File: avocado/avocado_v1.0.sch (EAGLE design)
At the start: 113 parts, among them IC1 TM4C129XXXPDT, IC3 MAX31855, IC4 ISO3088, J1 1X2-3.5MM, U1 LMT87DCKT

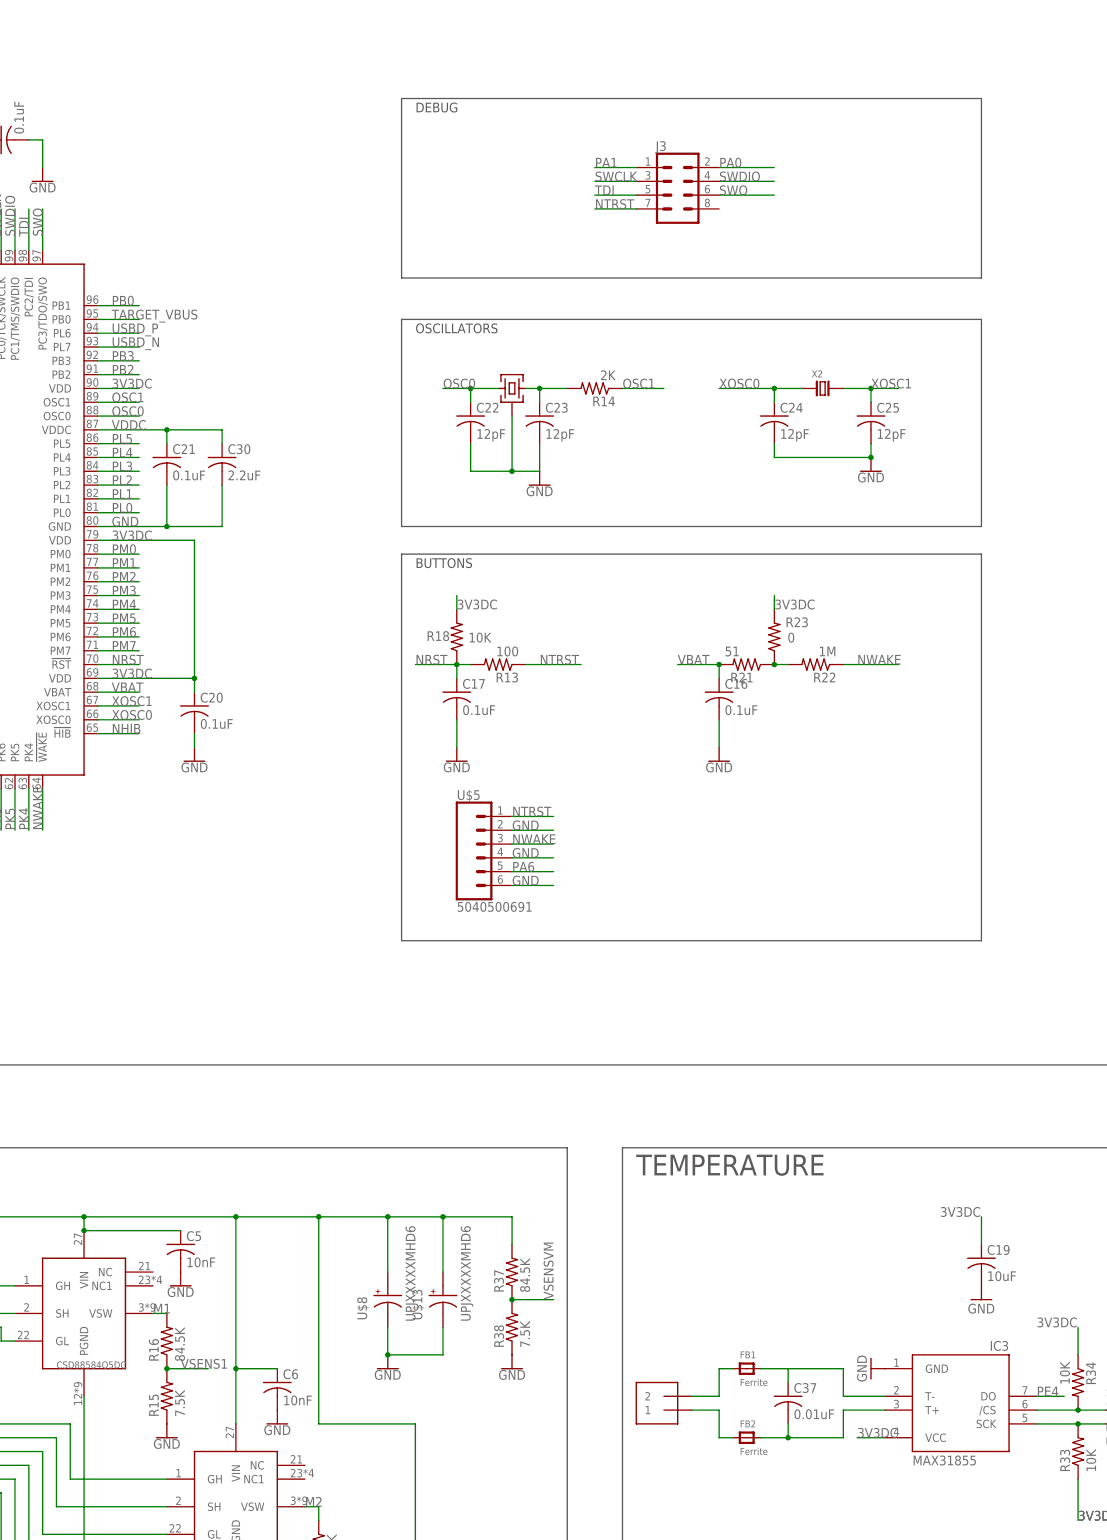
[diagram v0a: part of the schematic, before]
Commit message: expanded power and motor traces
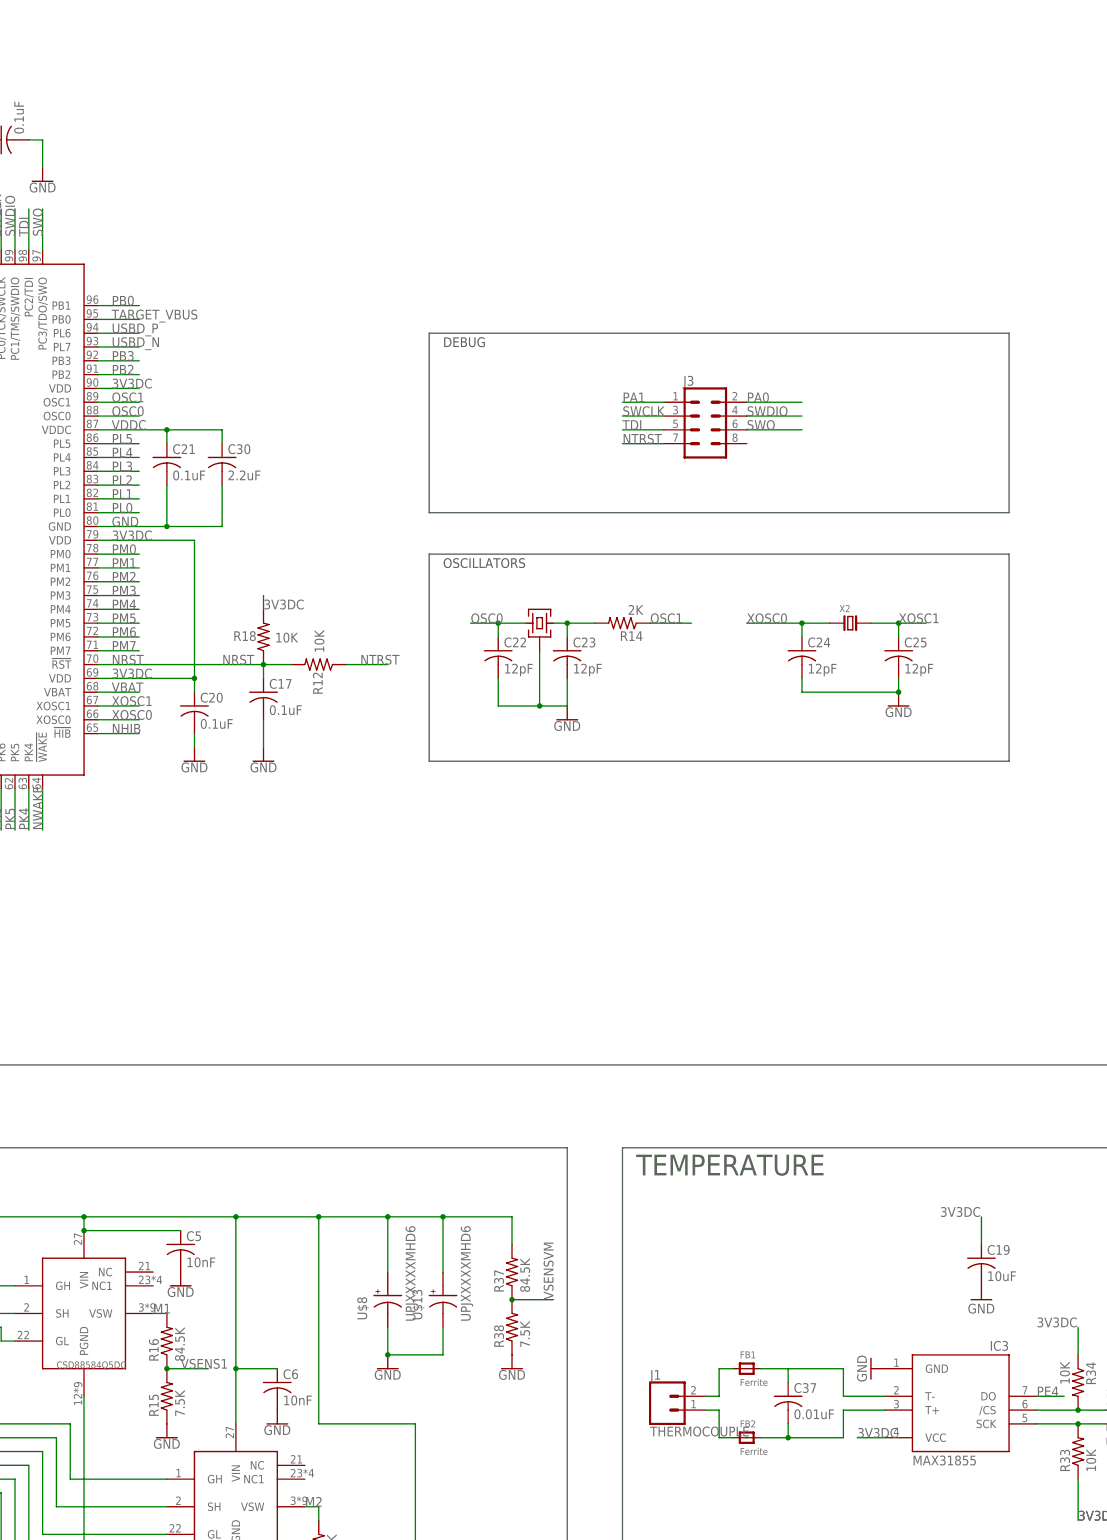
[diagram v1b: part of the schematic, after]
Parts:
- removed C16: 0.1uF, rcl:C-USC0402
- removed R13: 100, rcl:R-US_R0402
- removed R21: 51, rcl:R-US_R0402
- removed R22: 1M, rcl:R-US_R0402
- removed R23: 0, rcl:R-US_R0402
- removed U$5: 5040500691, avocado:5040500691
- added R12: 10K, rcl:R-US_R0402
- J1: value 1X2-3.5MM -> THERMOCOUPLE; device adafruit:1X2-3.5MM -> avocado:THERMOCOUPLE
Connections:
- removed net N$44: R21.1, R22.2, R23.1
- net 3V3DC: no longer R23.2
- net GND: no longer C16.2, U$5.2, U$5.4, U$5.6
- net NRST: now also R12.2; no longer R13.2
- net NTRST: now also R12.1; no longer R13.1, U$5.1
- net NWAKE: no longer R22.1, U$5.3
- net PA6: no longer U$5.5
- net VBAT: no longer C16.1, R21.2
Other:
- note removed: "BUTTONS"
- moved on the sheet: C17, C22, C23, C24, C25, J3, R14, R18, X2

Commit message: redesigned FET and Cap orientation
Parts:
- removed R15, R26, R36, R38: 7.5K, rcl:R-US_R0402
- removed R16, R17, R35, R37: 84.5K, rcl:R-US_R0402
- removed U$7: TPD4S009, avocado:TPD4S009
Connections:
- removed net VSENS1: IC1.PK0, R15.2, R16.1, U$7.D1+
- removed net VSENS2: IC1.PK1, R17.1, R26.2, U$7.D2+
- removed net VSENS3: IC1.PK2, R35.1, R36.2, U$7.D2-
- removed net VSENSVM: IC1.PE5, R37.1, R38.2, U$7.D1-
- new net PE5: IC1.PE5
- new net PK0: IC1.PK0
- new net PK1: IC1.PK1
- new net PK2: IC1.PK2
- net 24VDC: no longer R37.2
- net 3V3DC: no longer U$7.VCC
- net GND: no longer R15.1, R26.1, R36.1, R38.1, U$7.GND
- net M1: no longer R16.2
- net M2: no longer R17.2
- net M3: no longer R35.2
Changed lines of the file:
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@@
 <part name="GND33" library="SparkFun-PowerSymbols" deviceset="GND" device=""/>
 <part name="GND34" library="SparkFun-PowerSymbols" deviceset="GND" device=""/>
-<part name="R15" library="rcl" library_urn="urn:adsk.eagle:library:334" deviceset="R-US_" device="R0402" package3d_urn="urn:adsk.eagle:package:23547/2" value="7.5K"/>
-<part name="R16" library="rcl" library_urn="urn:adsk.eagle:library:334" deviceset="R-US_" device="R0402" package3d_urn="urn:adsk.eagle:package:23547/2" value="84.5K"/>
-<part name="GND35" library="SparkFun-PowerSymbols" deviceset="GND" device=""/>
-<part name="R17" library="rcl" library_urn="urn:adsk.eagle:library:334" deviceset="R-US_" device="R0402" package3d_urn="urn:adsk.eagle:package:23547/2" value="84.5K"/>
-<part name="R26" library="rcl" library_urn="urn:adsk.eagle:library:334" deviceset="R-US_" device="R0402" package3d_urn="urn:adsk.eagle:package:23547/2" value="7.5K"/>
-<part name="GND36" library="SparkFun-PowerSymbols" deviceset="GND" device=""/>
-<part name="R35" library="rcl" library_urn="urn:adsk.eagle:library:334" deviceset="R-US_" device="R0402" package3d_urn="urn:adsk.eagle:package:23547/2" value="84.5K"/>
-<part name="R36" library="rcl" library_urn="urn:adsk.eagle:library:334" deviceset="R-US_" device="R0402" package3d_urn="urn:adsk.eagle:package:23547/2" value="7.5K"/>
-<part name="GND37" library="SparkFun-PowerSymbols" deviceset="GND" device=""/>
-<part name="R37" library="rcl" library_urn="urn:adsk.eagle:library:334" deviceset="R-US_" device="R0402" package3d_urn="urn:adsk.eagle:package:23547/2" value="84.5K"/>
-<part name="R38" library="rcl" library_urn="urn:adsk.eagle:library:334" deviceset="R-US_" device="R0402" package3d_urn="urn:adsk.eagle:package:23547/2" value="7.5K"/>
-<part name="GND38" library="SparkFun-PowerSymbols" deviceset="GND" device=""/>
 <part name="C41" library="rcl" library_urn="urn:adsk.eagle:library:334" deviceset="C-US" device="C0402" package3d_urn="urn:adsk.eagle:package:23626/1" value="1000pF"/>
 <part name="C42" library="rcl" library_urn="urn:adsk.eagle:library:334" deviceset="C-US" device="C0402" package3d_urn="urn:adsk.eagle:package:23626/1" value="1000pF"/>
@@
 <part name="GND43" library="SparkFun-PowerSymbols" deviceset="GND" device=""/>
 <part name="GND44" library="SparkFun-PowerSymbols" deviceset="GND" device=""/>
-<part name="U$7" library="avocado" deviceset="TPD4S009" device=""/>
 <part name="GND45" library="SparkFun-PowerSymbols" deviceset="GND" device=""/>
 <part name="GND46" library="SparkFun-PowerSymbols" deviceset="GND" device=""/>
@@
 <instance part="GND33" gate="1" x="71.12" y="-104.14"/>
 <instance part="GND34" gate="1" x="104.14" y="-142.24"/>
-<instance part="R15" gate="G$1" x="50.8" y="-99.06" rot="R90"/>
-<instance part="R16" gate="G$1" x="50.8" y="-88.9" rot="R90"/>
-<instance part="GND35" gate="1" x="50.8" y="-106.68"/>
-<instance part="R17" gate="G$1" x="78.74" y="-127" rot="R90"/>
-<instance part="R26" gate="G$1" x="78.74" y="-137.16" rot="R90"/>
-<instance part="GND36" gate="1" x="78.74" y="-144.78"/>
-<instance part="R35" gate="G$1" x="111.76" y="-165.1" rot="R90"/>
-<instance part="R36" gate="G$1" x="111.76" y="-175.26" rot="R90"/>
-<instance part="GND37" gate="1" x="111.76" y="-182.88"/>
-<instance part="R37" gate="G$1" x="114.3" y="-76.2" rot="R90"/>
-<instance part="R38" gate="G$1" x="114.3" y="-86.36" rot="R90"/>
-<instance part="GND38" gate="1" x="114.3" y="-93.98"/>
 <instance part="C41" gate="G$1" x="-45.72" y="-177.8"/>
 <instance part="C42" gate="G$1" x="-53.34" y="-177.8"/>
@@
 <instance part="GND43" gate="1" x="-53.34" y="-190.5"/>
 <instance part="GND44" gate="1" x="-60.96" y="-190.5"/>
-<instance part="U$7" gate="G$1" x="-81.28" y="-114.3"/>
 <instance part="GND45" gate="1" x="-48.26" y="-147.32"/>
 <instance part="GND46" gate="1" x="-63.5" y="-147.32"/>
@@
 <wire x1="78.74" y1="-66.04" x2="91.44" y2="-66.04" width="0.1524" layer="91"/>
 <wire x1="91.44" y1="-66.04" x2="101.6" y2="-66.04" width="0.1524" layer="91"/>
-<wire x1="101.6" y1="-66.04" x2="114.3" y2="-66.04" width="0.1524" layer="91"/>
-<wire x1="114.3" y1="-66.04" x2="114.3" y2="-71.12" width="0.1524" layer="91"/>
-<pinref part="R37" gate="G$1" pin="2"/>
 <pinref part="U$8" gate="G$1" pin="A"/>
 <wire x1="91.44" y1="-66.04" x2="91.44" y2="-76.2" width="0.1524" layer="91"/>
@@
 <pinref part="U$13" gate="G$1" pin="A"/>
 <wire x1="101.6" y1="-66.04" x2="101.6" y2="-76.2" width="0.1524" layer="91"/>
-<junction x="101.6" y="-66.04"/>
 </segment>
 <segment>
@@
 </segment>
 <segment>
-<pinref part="R15" gate="G$1" pin="1"/>
-<pinref part="GND35" gate="1" pin="GND"/>
-</segment>
-<segment>
-<pinref part="R26" gate="G$1" pin="1"/>
-<pinref part="GND36" gate="1" pin="GND"/>
-</segment>
-<segment>
-<pinref part="R36" gate="G$1" pin="1"/>
-<pinref part="GND37" gate="1" pin="GND"/>
-</segment>
-<segment>
-<pinref part="R38" gate="G$1" pin="1"/>
-<pinref part="GND38" gate="1" pin="GND"/>
-</segment>
-<segment>
 <pinref part="R6" gate="G$1" pin="1"/>
 <pinref part="GND39" gate="1" pin="GND"/>
@@
 <wire x1="-63.5" y1="-139.7" x2="-63.5" y2="-144.78" width="0.1524" layer="91"/>
 <pinref part="GND46" gate="1" pin="GND"/>
-</segment>
-<segment>
-<pinref part="U$7" gate="G$1" pin="GND"/>
-<wire x1="-93.98" y1="-114.3" x2="-99.06" y2="-114.3" width="0.1524" layer="91"/>
-<label x="-101.6" y="-114.3" size="1.778" layer="95"/>
 </segment>
 <segment>
@@
 </segment>
 <segment>
-<pinref part="U$7" gate="G$1" pin="VCC"/>
-<wire x1="-68.58" y1="-114.3" x2="-60.96" y2="-114.3" width="0.1524" layer="91"/>
-<label x="-68.58" y="-114.3" size="1.778" layer="95"/>
-</segment>
-<segment>
 <pinref part="U$1" gate="G$1" pin="P$2"/>
 <wire x1="-165.1" y1="-5.08" x2="-154.94" y2="-5.08" width="0.1524" layer="91"/>
@@
 <wire x1="48.26" y1="-83.82" x2="50.8" y2="-83.82" width="0.1524" layer="91"/>
 <label x="48.26" y="-83.82" size="1.778" layer="95"/>
-<pinref part="R16" gate="G$1" pin="2"/>
 </segment>
 <segment>
@@
 <wire x1="76.2" y1="-119.38" x2="78.74" y2="-119.38" width="0.1524" layer="91"/>
 <label x="76.2" y="-119.38" size="1.778" layer="95"/>
-<pinref part="R17" gate="G$1" pin="2"/>
-<wire x1="78.74" y1="-121.92" x2="78.74" y2="-119.38" width="0.1524" layer="91"/>
 </segment>
 </net>
@@
 <pinref part="U$10" gate="G$1" pin="VSW"/>
 <wire x1="109.22" y1="-157.48" x2="111.76" y2="-157.48" width="0.1524" layer="91"/>
-<pinref part="R35" gate="G$1" pin="2"/>
-<wire x1="111.76" y1="-157.48" x2="111.76" y2="-160.02" width="0.1524" layer="91"/>
 <label x="109.22" y="-157.48" size="1.778" layer="95"/>
 </segment>
@@
 </segment>
 </net>
-<net name="VSENS1" class="0">
-<segment>
-<pinref part="R16" gate="G$1" pin="1"/>
-<pinref part="R15" gate="G$1" pin="2"/>
-<wire x1="50.8" y1="-93.98" x2="58.42" y2="-93.98" width="0.1524" layer="91"/>
-<junction x="50.8" y="-93.98"/>
-<label x="53.34" y="-93.98" size="1.778" layer="95"/>
-</segment>
-<segment>
-<pinref part="U$7" gate="G$1" pin="D1+"/>
-<wire x1="-93.98" y1="-109.22" x2="-99.06" y2="-109.22" width="0.1524" layer="91"/>
-<label x="-101.6" y="-109.22" size="1.778" layer="95"/>
-</segment>
+<net name="PK0" class="0">
 <segment>
 <pinref part="IC1" gate="G$1" pin="PK0"/>
@@
 </segment>
 </net>
-<net name="VSENS2" class="0">
-<segment>
-<pinref part="R17" gate="G$1" pin="1"/>
-<pinref part="R26" gate="G$1" pin="2"/>
-<wire x1="78.74" y1="-132.08" x2="86.36" y2="-132.08" width="0.1524" layer="91"/>
-<junction x="78.74" y="-132.08"/>
-<label x="83.82" y="-132.08" size="1.778" layer="95"/>
-</segment>
-<segment>
-<pinref part="U$7" gate="G$1" pin="D2+"/>
-<wire x1="-93.98" y1="-119.38" x2="-99.06" y2="-119.38" width="0.1524" layer="91"/>
-<label x="-101.6" y="-119.38" size="1.778" layer="95"/>
-</segment>
+<net name="PK1" class="0">
 <segment>
 <pinref part="IC1" gate="G$1" pin="PK1"/>
@@
 </segment>
 </net>
-<net name="VSENS3" class="0">
-<segment>
-<pinref part="R35" gate="G$1" pin="1"/>
-<pinref part="R36" gate="G$1" pin="2"/>
-<wire x1="111.76" y1="-170.18" x2="116.84" y2="-170.18" width="0.1524" layer="91"/>
-<junction x="111.76" y="-170.18"/>
-<label x="114.3" y="-170.18" size="1.778" layer="95"/>
-</segment>
-<segment>
-<pinref part="U$7" gate="G$1" pin="D2-"/>
-<wire x1="-68.58" y1="-119.38" x2="-60.96" y2="-119.38" width="0.1524" layer="91"/>
-<label x="-68.58" y="-119.38" size="1.778" layer="95"/>
-</segment>
+<net name="PK2" class="0">
 <segment>
 <pinref part="IC1" gate="G$1" pin="PK2"/>
@@
 </segment>
 </net>
-<net name="VSENSVM" class="0">
-<segment>
-<pinref part="R37" gate="G$1" pin="1"/>
-<pinref part="R38" gate="G$1" pin="2"/>
-<wire x1="114.3" y1="-81.28" x2="121.92" y2="-81.28" width="0.1524" layer="91"/>
-<junction x="114.3" y="-81.28"/>
-<label x="121.92" y="-81.28" size="1.778" layer="95" rot="R90"/>
-</segment>
-<segment>
-<pinref part="U$7" gate="G$1" pin="D1-"/>
-<wire x1="-68.58" y1="-109.22" x2="-60.96" y2="-109.22" width="0.1524" layer="91"/>
-<label x="-68.58" y="-109.22" size="1.778" layer="95"/>
-</segment>
+<net name="PE5" class="0">
 <segment>
 <pinref part="IC1" gate="G$1" pin="PE5"/>

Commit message: finished DRC and silk for version 1
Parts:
- removed U$1: 0522070633, avocado:0522070633
- added U$5: 5040500591, avocado:5040500591
- renumbered 3V3BUCK to U$6, 5VBUCK to U$7, SRU1028-101Y to L2, SRU1028-151Y to L1
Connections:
- net 3V3DC: now also U$5.1; no longer U$1.P$2
- net A: now also U$5.4; no longer U$1.P$6
- net B: now also U$5.5; no longer U$1.P$5
- net GND: now also U$5.2; no longer U$1.P$3
- net GND_EXT: now also U$5.3; no longer U$1.P$4
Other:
- moved on the sheet: U$3

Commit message: design that was ordered in first PCB run
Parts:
- renumbered U$13 to C51, U$8 to C50
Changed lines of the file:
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@@
 <part name="GND45" library="SparkFun-PowerSymbols" deviceset="GND" device=""/>
 <part name="GND46" library="SparkFun-PowerSymbols" deviceset="GND" device=""/>
-<part name="U$8" library="avocado" deviceset="UPJXXXXXMHD6" device=""/>
-<part name="U$13" library="avocado" deviceset="UPJXXXXXMHD6" device=""/>
+<part name="C50" library="avocado" deviceset="UPJXXXXXMHD6" device=""/>
+<part name="C51" library="avocado" deviceset="UPJXXXXXMHD6" device=""/>
 <part name="GND47" library="SparkFun-PowerSymbols" deviceset="GND" device=""/>
 <part name="U$2" library="avocado" deviceset="0522070633" device=""/>
@@
 <instance part="GND45" gate="1" x="-48.26" y="-147.32"/>
 <instance part="GND46" gate="1" x="-63.5" y="-147.32"/>
-<instance part="U$8" gate="G$1" x="91.44" y="-81.28"/>
-<instance part="U$13" gate="G$1" x="101.6" y="-81.28"/>
+<instance part="C50" gate="G$1" x="91.44" y="-81.28"/>
+<instance part="C51" gate="G$1" x="101.6" y="-81.28"/>
 <instance part="GND47" gate="1" x="91.44" y="-93.98"/>
 <instance part="U$2" gate="G$1" x="-210.82" y="-93.98"/>
@@
 <wire x1="78.74" y1="-66.04" x2="91.44" y2="-66.04" width="0.1524" layer="91"/>
 <wire x1="91.44" y1="-66.04" x2="101.6" y2="-66.04" width="0.1524" layer="91"/>
-<pinref part="U$8" gate="G$1" pin="A"/>
+<pinref part="C50" gate="G$1" pin="A"/>
 <wire x1="91.44" y1="-66.04" x2="91.44" y2="-76.2" width="0.1524" layer="91"/>
 <junction x="91.44" y="-66.04"/>
-<pinref part="U$13" gate="G$1" pin="A"/>
+<pinref part="C51" gate="G$1" pin="A"/>
 <wire x1="101.6" y1="-66.04" x2="101.6" y2="-76.2" width="0.1524" layer="91"/>
 </segment>
@@
 </segment>
 <segment>
-<pinref part="U$8" gate="G$1" pin="C"/>
+<pinref part="C50" gate="G$1" pin="C"/>
 <pinref part="GND47" gate="1" pin="GND"/>
 <wire x1="91.44" y1="-86.36" x2="91.44" y2="-91.44" width="0.1524" layer="91"/>
-<pinref part="U$13" gate="G$1" pin="C"/>
+<pinref part="C51" gate="G$1" pin="C"/>
 <wire x1="101.6" y1="-86.36" x2="101.6" y2="-91.44" width="0.1524" layer="91"/>
 <wire x1="101.6" y1="-91.44" x2="91.44" y2="-91.44" width="0.1524" layer="91"/>
